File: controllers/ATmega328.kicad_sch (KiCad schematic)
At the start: 10 parts, among them U401 ATMEGA328P-AU, Y407 16MHz

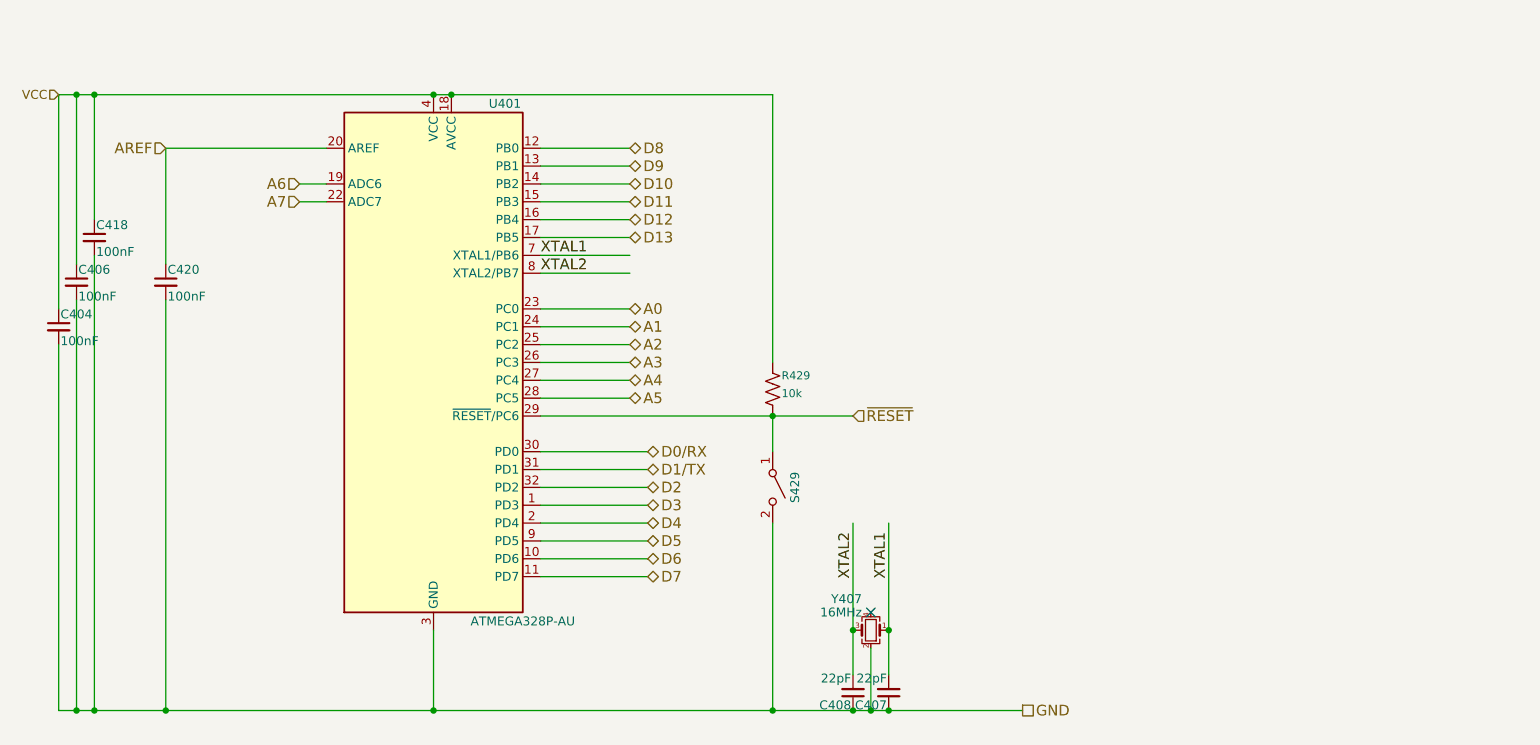
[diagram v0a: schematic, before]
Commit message: Changed analog and digital I/O to buses
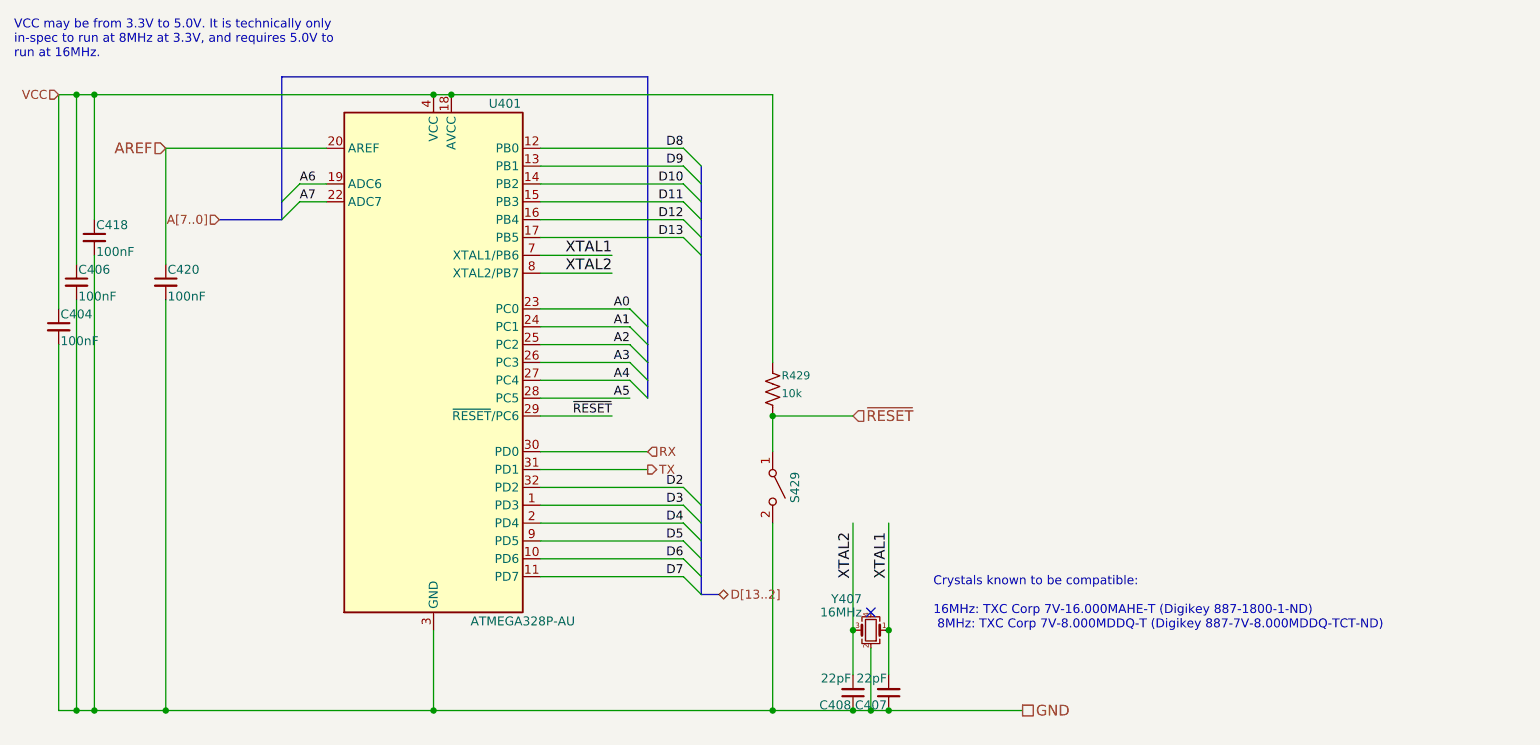
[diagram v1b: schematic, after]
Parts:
- C404, C406, C407, C408, C418, C420: footprint Capacitor_SMD:C_0402_1005Metric -> Capacitor_SMD:C_0603_1608Metric
- R429: footprint Resistor_SMD:R_0402_1005Metric -> Resistor_SMD:R_0603_1608Metric
- Y407: footprint Crystals:Crystal_SMD_2520-4pin_2.5x2.0mm -> Crystal:Crystal_SMD_3225-4Pin_3.2x2.5mm; Digikey 535-9675-1-ND -> 887-1800-1-ND
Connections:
- net D0/RX renamed RX
- net D1/TX renamed TX
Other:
- note added: "Crystals known to be compatible: 16MHz: TXC Corp 7V-16.000MAHE-T (Digikey 887-1800-1-ND) 8MHz: TXC Corp 7V-8.000MDDQ-T (Digikey 887-7V-8.000MDDQ-TCT-ND)"
- note added: "VCC may be from 3.3V to 5.0V. It is technically only in-spec to run at 8MHz at 3.3V, and requires 5.0V to run at 16MHz."

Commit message: Added labels for alternate purposes of pins
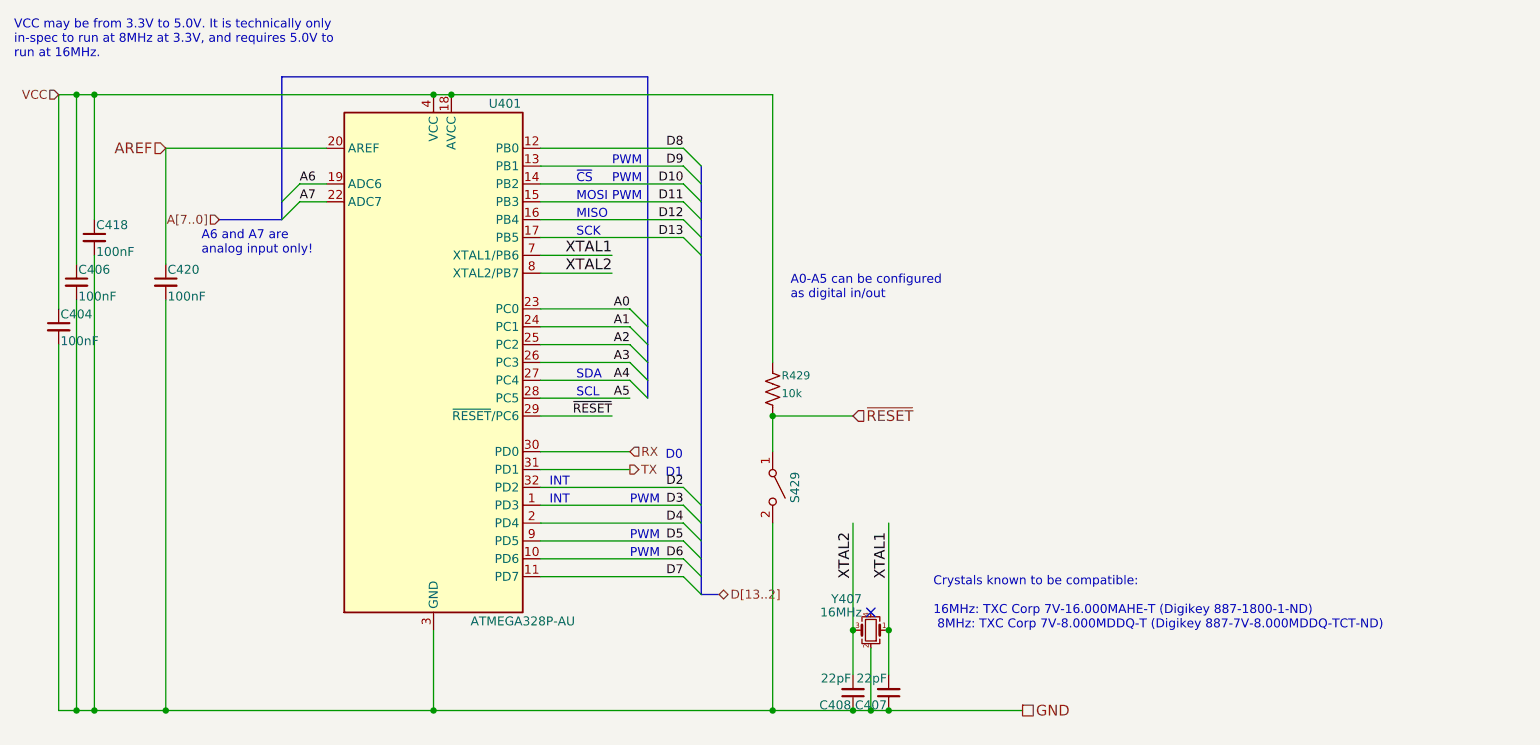
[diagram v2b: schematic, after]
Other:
- note added: "A0-A5 can be configured as digital in/out"
- note added: "A6 and A7 are analog input only!"
- note added: "D0"
- note added: "D1"
- note added: "INT"
- note added: "MISO"
- note added: "MOSI"
- note added: "PWM"
- note added: "SCK"
- note added: "SCL"
- note added: "SDA"
- note added: "~{CS}"
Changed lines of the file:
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@@
     (stroke (width 0) (type default))
   )
-  (wire (pts (xy 91.44 76.2) (xy 106.68 76.2))
+  (wire (pts (xy 91.44 76.2) (xy 104.14 76.2))
     (stroke (width 0) (type default))
   )
@@
     (stroke (width 0) (type default))
   )
-  (wire (pts (xy 91.44 78.74) (xy 106.68 78.74))
+  (wire (pts (xy 91.44 78.74) (xy 104.14 78.74))
     (stroke (width 0) (type default))
   )
@@
   (wire (pts (xy 138.43 113.03) (xy 140.97 113.03))
     (stroke (width 0) (type default))
+  )
+  (text "D1" (at 109.22 80.01 0)
+    (effects (font (size 1.27 1.27)) (justify left bottom))
+  )
+  (text "PWM" (at 104.14 91.44 0)
+    (effects (font (size 1.27 1.27)) (justify left bottom))
+  )
+  (text "D0" (at 109.22 77.47 0)
+    (effects (font (size 1.27 1.27)) (justify left bottom))
+  )
+  (text "A0-A5 can be configured\nas digital in/out" (at 127 54.61 0)
+    (effects (font (size 1.27 1.27)) (justify left bottom))
   )
   (text "Crystals known to be compatible:\n\n16MHz: TXC Corp 7V-16.000MAHE-T (Digikey 887-1800-1-ND)\n 8MHz: TXC Corp 7V-8.000MDDQ-T (Digikey 887-7V-8.000MDDQ-TCT-ND)"
@@
     (effects (font (size 1.27 1.27)) (justify left bottom))
   )
+  (text "A6 and A7 are\nanalog input only!" (at 43.18 48.26 0)
+    (effects (font (size 1.27 1.27)) (justify left bottom))
+  )
+  (text "PWM" (at 104.14 88.9 0)
+    (effects (font (size 1.27 1.27)) (justify left bottom))
+  )
+  (text "PWM" (at 101.6 40.64 0)
+    (effects (font (size 1.27 1.27)) (justify left bottom))
+  )
+  (text "SCL" (at 96.52 68.58 0)
+    (effects (font (size 1.27 1.27)) (justify left bottom))
+  )
+  (text "MOSI" (at 96.52 40.64 0)
+    (effects (font (size 1.27 1.27)) (justify left bottom))
+  )
+  (text "INT" (at 92.71 81.28 0)
+    (effects (font (size 1.27 1.27)) (justify left bottom))
+  )
   (text "VCC may be from 3.3V to 5.0V. It is technically only\nin-spec to run at 8MHz at 3.3V, and requires 5.0V to\nrun at 16MHz."
     (at 16.51 20.32 0)
     (effects (font (size 1.27 1.27)) (justify left bottom))
   )
+  (text "PWM" (at 101.6 38.1 0)
+    (effects (font (size 1.27 1.27)) (justify left bottom))
+  )
+  (text "~{CS}" (at 96.52 38.1 0)
+    (effects (font (size 1.27 1.27)) (justify left bottom))
+  )
+  (text "SDA" (at 96.52 66.04 0)
+    (effects (font (size 1.27 1.27)) (justify left bottom))
+  )
+  (text "MISO" (at 96.52 43.18 0)
+    (effects (font (size 1.27 1.27)) (justify left bottom))
+  )
+  (text "SCK" (at 96.52 45.72 0)
+    (effects (font (size 1.27 1.27)) (justify left bottom))
+  )
+  (text "INT" (at 92.71 83.82 0)
+    (effects (font (size 1.27 1.27)) (justify left bottom))
+  )
+  (text "PWM" (at 104.14 83.82 0)
+    (effects (font (size 1.27 1.27)) (justify left bottom))
+  )
+  (text "PWM" (at 101.6 35.56 0)
+    (effects (font (size 1.27 1.27)) (justify left bottom))
+  )
   (label "XTAL2" (at 135.89 87.63 270) (fields_autoplaced)
     (effects (font (size 1.524 1.524)) (justify right bottom))
@@
     (effects (font (size 1.524 1.524)) (justify right))
   )
-  (hierarchical_label "RX" (shape input) (at 106.68 76.2 0) (fields_autoplaced)
+  (hierarchical_label "RX" (shape input) (at 104.14 76.2 0) (fields_autoplaced)
     (effects (font (size 1.27 1.27)) (justify left))
   )
@@
     (effects (font (size 1.524 1.524)) (justify left))
   )
-  (hierarchical_label "TX" (shape output) (at 106.68 78.74 0) (fields_autoplaced)
+  (hierarchical_label "TX" (shape output) (at 104.14 78.74 0) (fields_autoplaced)
     (effects (font (size 1.27 1.27)) (justify left))
   )
